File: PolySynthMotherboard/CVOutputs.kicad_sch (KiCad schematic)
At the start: 154 parts, among them U301 DAC7578xPW, U302 TL074, U303 TL072, U304 TMUX4051, U305 TL074, U306 TMUX4051, U307 TL074, U308 TMUX4051, U309 TMUX4051, U310 TL074, U311 TL074, U312 TL074, U313 TMUX4051, U314 TL074, U315 TL074, U316 TL074, U317 TMUX4051, U318 TMUX4051, U319 TL074, U320 TL072

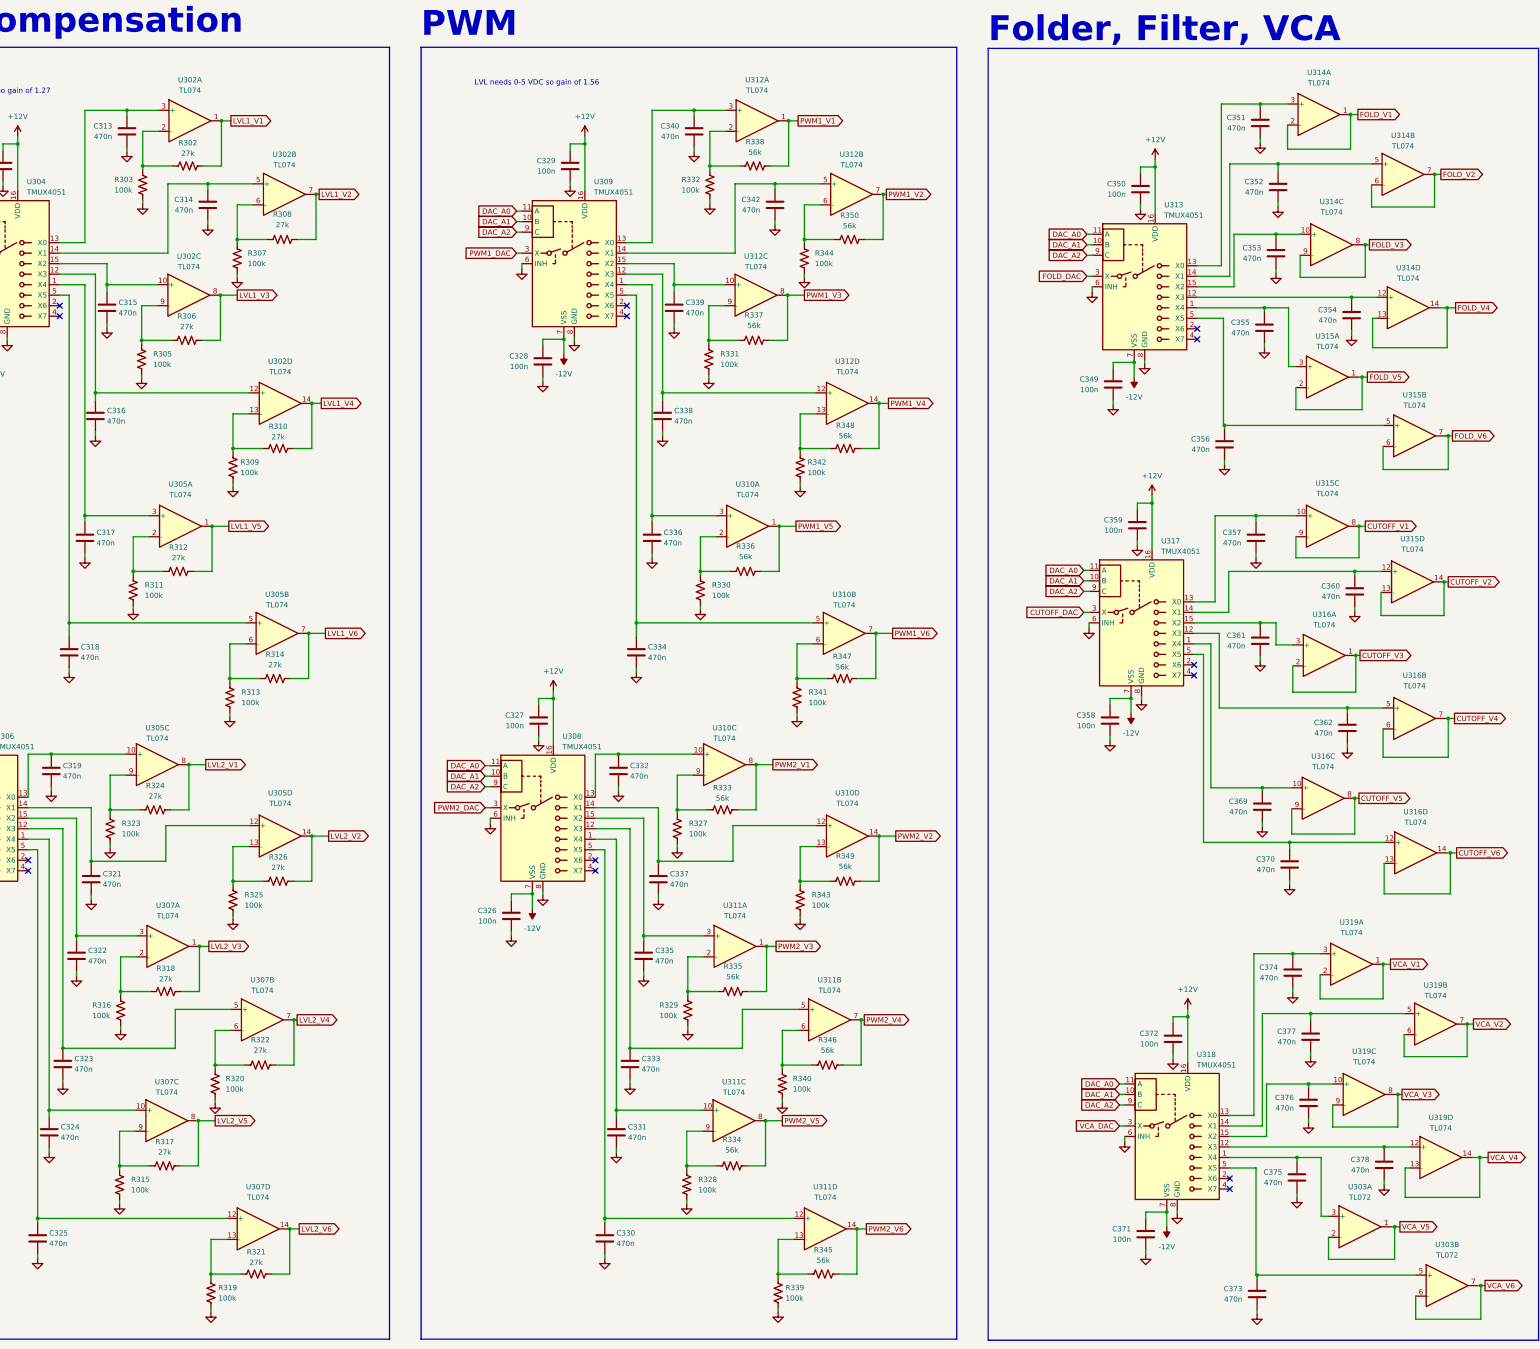
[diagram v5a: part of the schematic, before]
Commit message: op-amp layout improved
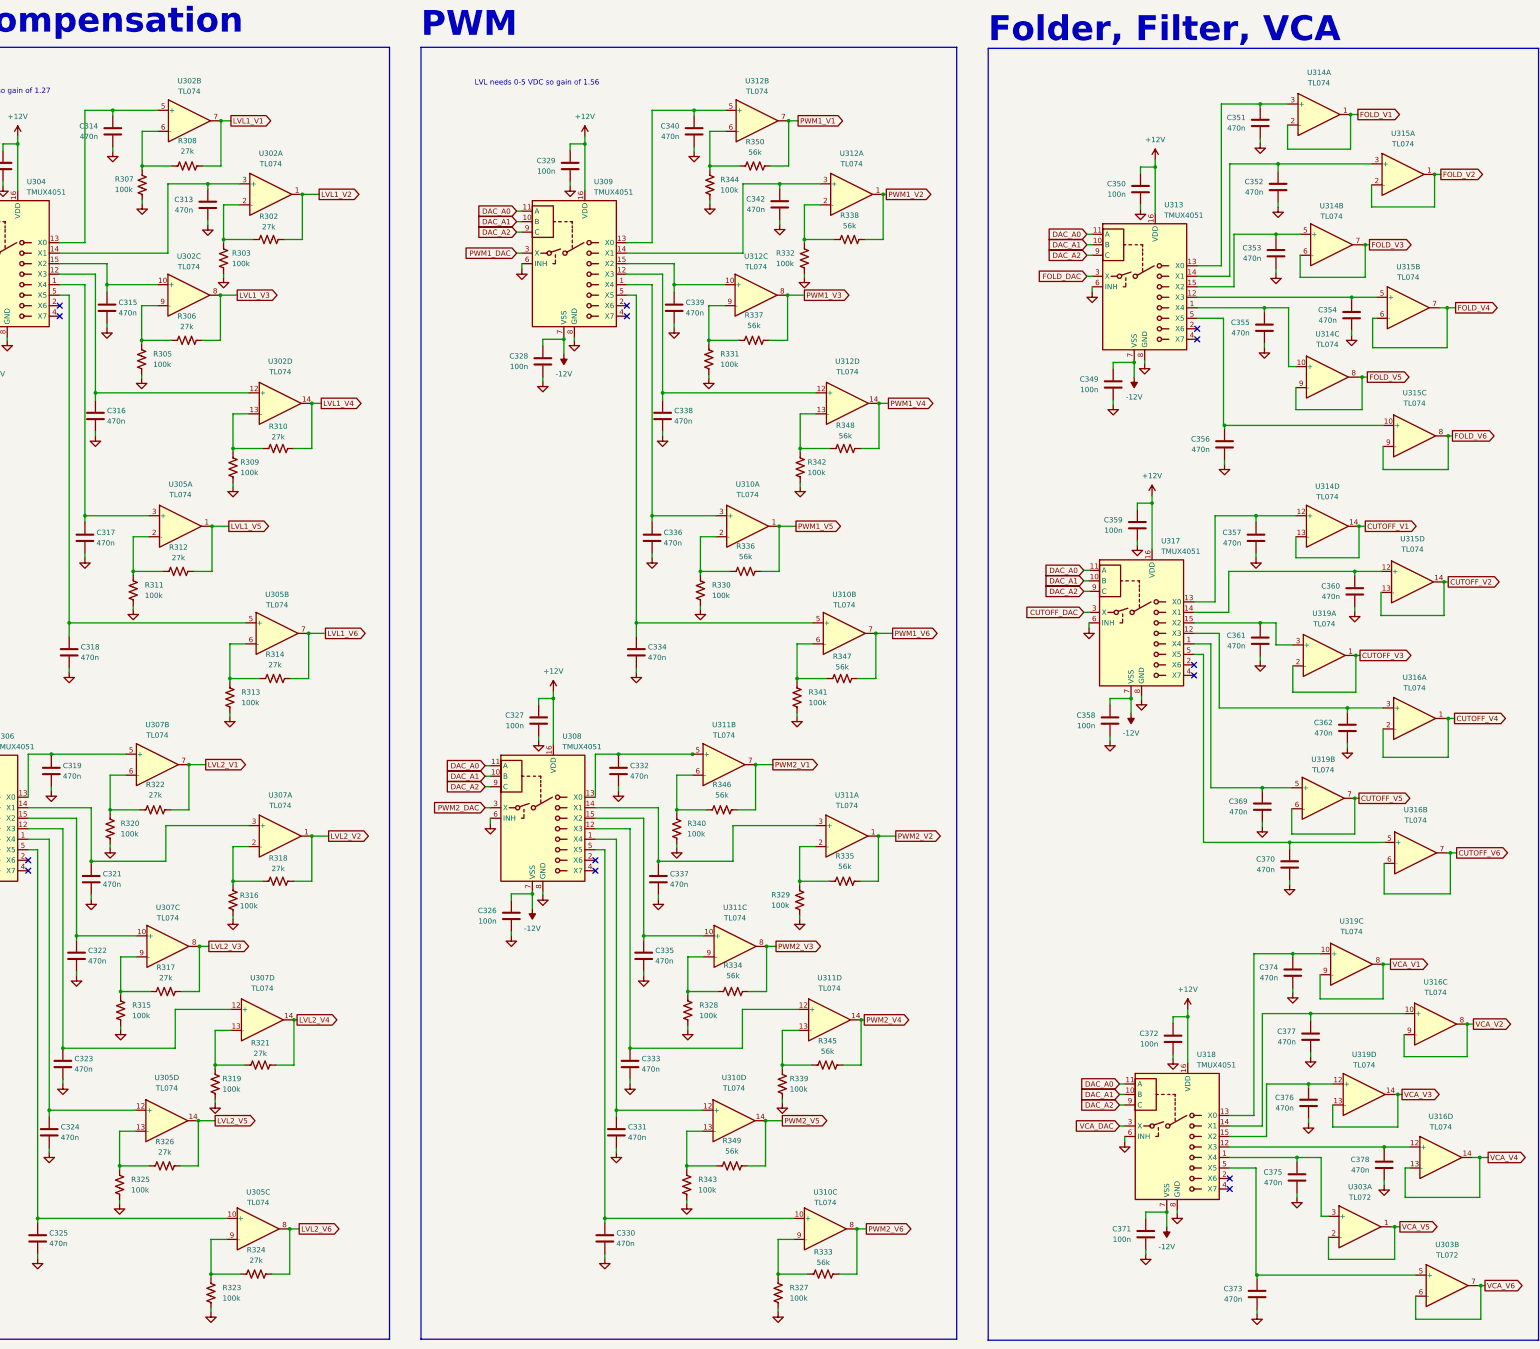
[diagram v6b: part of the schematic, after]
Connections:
- net CUTOFF_V1: now also U314.13 (-), U314.14; no longer U315.8, U315.9 (-)
- net CUTOFF_V3: now also U319.1, U319.2 (-); no longer U316.1, U316.2 (-)
- net CUTOFF_V4: now also U316.1, U316.2 (-); no longer U316.6 (-), U316.7
- net CUTOFF_V5: now also U319.6 (-), U319.7; no longer U316.8, U316.9 (-)
- net CUTOFF_V6: now also U316.6 (-), U316.7; no longer U316.13 (-), U316.14
- net FOLD_V2: now also U315.1, U315.2 (-); no longer U314.6 (-), U314.7
- net FOLD_V3: now also U314.6 (-), U314.7; no longer U314.8, U314.9 (-)
- net FOLD_V4: now also U315.6 (-), U315.7; no longer U314.13 (-), U314.14
- net FOLD_V5: now also U314.8, U314.9 (-); no longer U315.1, U315.2 (-)
- net FOLD_V6: now also U315.8, U315.9 (-); no longer U315.6 (-), U315.7
- net LVL1_V1: now also R308.2, U302.7; no longer R302.2, U302.1
- net LVL1_V2: now also R302.2, U302.1; no longer R308.2, U302.7
- net LVL2_V1: now also R322.2, U307.7; no longer R324.2, U305.8
- net LVL2_V2: now also R318.2, U307.1; no longer R326.2, U305.14
- net LVL2_V3: now also R317.2, U307.8; no longer R318.2, U307.1
- net LVL2_V4: now also R321.2, U307.14; no longer R322.2, U307.7
- net LVL2_V5: now also R326.2, U305.14; no longer R317.2, U307.8
- net LVL2_V6: now also R324.2, U305.8; no longer R321.2, U307.14
- net PWM1_V1: now also R350.2, U312.7; no longer R338.2, U312.1
- net PWM1_V2: now also R338.2, U312.1; no longer R350.2, U312.7
- net PWM2_V1: now also R346.2, U311.7; no longer R333.2, U310.8
- net PWM2_V2: now also R335.2, U311.1; no longer R349.2, U310.14
- net PWM2_V3: now also R334.2, U311.8; no longer R335.2, U311.1
- net PWM2_V4: now also R345.2, U311.14; no longer R346.2, U311.7
- net PWM2_V5: now also R349.2, U310.14; no longer R334.2, U311.8
- net PWM2_V6: now also R333.2, U310.8; no longer R345.2, U311.14
- net VCA_V1: now also U319.8, U319.9 (-); no longer U319.1, U319.2 (-)
- net VCA_V2: now also U316.8, U316.9 (-); no longer U319.6 (-), U319.7
- net VCA_V3: now also U319.13 (-), U319.14; no longer U319.8, U319.9 (-)
- net VCA_V4: now also U316.13 (-), U316.14; no longer U319.13 (-), U319.14
- net at C361.1, U317.15 (X2): now also U319.3 (+); no longer U316.3 (+)
- net at C321.1, U306.14 (X1): now also U307.3 (+); no longer U305.12 (+)
- net at C377.1, U318.14 (X1): now also U316.10 (+); no longer U319.5 (+)
- net at C314.1, U302.5 (+): now also U304.13 (X0); no longer U304.14 (X1)
- net at C322.1, U306.15 (X2): now also U307.10 (+); no longer U307.3 (+)
- net at C369.1, U317.1 (X4): now also U319.5 (+); no longer U316.10 (+)
- net at C352.1, U313.14 (X1): now also U315.3 (+); no longer U314.5 (+)
- net at C362.1, U317.12 (X3): now also U316.3 (+); no longer U316.5 (+)
- net at C330.1, U308.5 (X5): now also U310.10 (+); no longer U311.12 (+)
- net at C354.1, U313.12 (X3): now also U315.5 (+); no longer U314.12 (+)
- net at C356.1, U313.5 (X5): now also U315.10 (+); no longer U315.5 (+)
- net at C313.1, U302.3 (+): now also U304.14 (X1); no longer U304.13 (X0)
- net at C319.1, U306.13 (X0): now also U307.5 (+); no longer U305.10 (+)
- net at C324.1, U306.1 (X4): now also U305.12 (+); no longer U307.10 (+)
- net at C331.1, U308.1 (X4): now also U310.12 (+); no longer U311.10 (+)
- net at C335.1, U308.15 (X2): now also U311.10 (+); no longer U311.3 (+)
- net at C325.1, U306.5 (X5): now also U305.10 (+); no longer U307.12 (+)
- net at C337.1, U308.14 (X1): now also U311.3 (+); no longer U310.12 (+)
- net at C340.1, U309.13 (X0): now also U312.5 (+); no longer U312.3 (+)
- net at C323.1, U306.12 (X3): now also U307.12 (+); no longer U307.5 (+)
- net at C378.1, U318.12 (X3): now also U316.12 (+); no longer U319.12 (+)
- net at C374.1, U318.13 (X0): now also U319.10 (+); no longer U319.3 (+)
- net at C376.1, U318.15 (X2): now also U319.12 (+); no longer U319.10 (+)
- net at C353.1, U313.15 (X2): now also U314.5 (+); no longer U314.10 (+)
- net at C355.1, U313.1 (X4): now also U314.10 (+); no longer U315.3 (+)
- net at C342.1, U309.14 (X1): now also U312.3 (+); no longer U312.5 (+)
- net at C333.1, U308.12 (X3): now also U311.12 (+); no longer U311.5 (+)
- net at C370.1, U317.5 (X5): now also U316.5 (+); no longer U316.12 (+)
- net at C357.1, U317.13 (X0): now also U314.12 (+); no longer U315.10 (+)
- net at C332.1, U308.13 (X0): now also U311.5 (+); no longer U310.10 (+)
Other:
- moved on the sheet: C313, C314, C342, R302, R303, R307, R308, R315, R316, R317, R318, R319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

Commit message: power supply tweaks
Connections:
- net FOLD_V3: now also U314.8, U314.9 (-); no longer U314.6 (-), U314.7
- net FOLD_V5: now also U314.6 (-), U314.7; no longer U314.8, U314.9 (-)
- net GND: no longer U304.6 (INH), U306.6 (INH), U308.6 (INH), U309.6 (INH), U313.6 (INH), U317.6 (INH), U318.6 (INH)
- net PWM2_V1: now also R335.2, U311.1; no longer R346.2, U311.7
- net PWM2_V2: now also R346.2, U311.7; no longer R335.2, U311.1
- net PWM2_V3: now also R345.2, U311.14; no longer R334.2, U311.8
- net PWM2_V4: now also R334.2, U311.8; no longer R345.2, U311.14
- net at C353.1, U314.5 (+): now also U313.1 (X4); no longer U313.15 (X2)
- net at C333.1, U308.12 (X3): now also U311.10 (+); no longer U311.12 (+)
- net at C335.1, U308.15 (X2): now also U311.12 (+); no longer U311.10 (+)
- net at C337.1, U308.14 (X1): now also U311.5 (+); no longer U311.3 (+)
- net at C355.1, U314.10 (+): now also U313.15 (X2); no longer U313.1 (X4)
- net at C332.1, U308.13 (X0): now also U311.3 (+); no longer U311.5 (+)
- new net DAC_INH: U304.6 (INH), U306.6 (INH), U308.6 (INH), U309.6 (INH), U313.6 (INH), U317.6 (INH), U318.6 (INH)
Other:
- moved on the sheet: C353, C355, R328, R329, R334, R335, R339, R340, R345, R346, U311A, U311B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

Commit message: cleaned up CV opamps
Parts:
- removed R302, R306, R308, R310, R312, R314, R317, R318, R321, R322, R324, R326: 27k, PCM_Resistor_SMD_AKL:R_0805_2012Metric, symbol Device:R_US
- removed R303, R305, R307, R309, R311, R313, R315, R316, R319, R320, R323, R325, R327, R328, R329, R330, R331, R332, R339, R340, R341, R342, R343, R344: 100k, PCM_Resistor_SMD_AKL:R_0805_2012Metric, symbol Device:R_US
- removed R333, R334, R335, R336, R337, R338, R345, R346, R347, R348, R349, R350: 56k, PCM_Resistor_SMD_AKL:R_0805_2012Metric, symbol Device:R_US
- added C320, C341: 100n, Capacitor_SMD:C_0805_2012Metric, symbol Device:C
- added R351, R353, R355, R357: 100k, PCM_Resistor_SMD_AKL:R_0805_2012Metric, symbol Device:R_US
- added R352, R354: 27k, PCM_Resistor_SMD_AKL:R_0805_2012Metric, symbol Device:R_US
- added R356, R358: 56k, PCM_Resistor_SMD_AKL:R_0805_2012Metric, symbol Device:R_US
- added U321: TL074, Package_SO:SOIC-14_3.9x8.7mm_P1.27mm, symbol Amplifier_Operational:TL074
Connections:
- net +3.3VA is gone; now on net +3.3V: C301.1, C304.1, R304.1, U301.3 (AVDD)
- net +12V: now also C320.1, U321.4 (V+)
- net -12V: now also C341.1, U321.11 (V-)
- net CUTOFF_V1: now also U305.6 (-), U305.7; no longer U314.13 (-), U314.14
- net CUTOFF_V2: now also U310.6 (-), U310.7; no longer U315.13 (-), U315.14
- net CUTOFF_V3: now also U311.13 (-), U311.14; no longer U319.1, U319.2 (-)
- net CUTOFF_V4: now also U314.8, U314.9 (-); no longer U316.1, U316.2 (-)
- net CUTOFF_V5: now also U316.6 (-), U316.7; no longer U319.6 (-), U319.7
- net CUTOFF_V6: now also U319.13 (-), U319.14; no longer U316.6 (-), U316.7
- net FOLD_V1: now also U305.1, U305.2 (-); no longer U314.1, U314.2 (-)
- net FOLD_V2: now also U310.1, U310.2 (-); no longer U315.1, U315.2 (-)
- net FOLD_V3: now also U311.8, U311.9 (-); no longer U314.8, U314.9 (-)
- net FOLD_V4: now also U314.6 (-), U314.7; no longer U315.6 (-), U315.7
- net FOLD_V5: now also U316.1, U316.2 (-); no longer U314.6 (-), U314.7
- net FOLD_V6: now also U319.8, U319.9 (-); no longer U315.8, U315.9 (-)
- net GND: now also C320.2, C341.2, R351.1, R353.1, R355.1, R357.1
- net LVL1_DAC: now also R352.2, U321.1; no longer U301.4 (VOUTA)
- net LVL1_V1: now also U302.6 (-)
- net LVL1_V2: now also U307.1, U307.2 (-); no longer U302.1
- net LVL1_V3: now also U310.8, U310.9 (-); no longer U302.8
- net LVL1_V4: now also U312.6 (-), U312.7; no longer U302.14
- net LVL1_V5: now also U315.1, U315.2 (-); no longer U305.1
- net LVL1_V6: now also U316.8, U316.9 (-); no longer U305.7
- net LVL2_DAC: now also R354.2, U321.7; no longer U301.13 (VOUTB)
- net LVL2_V1: now also U302.1, U302.2 (-); no longer U307.7
- net LVL2_V2: now also U307.6 (-), U307.7; no longer U307.1
- net LVL2_V3: now also U310.13 (-), U310.14; no longer U307.8
- net LVL2_V4: now also U312.8, U312.9 (-); no longer U307.14
- net LVL2_V5: now also U315.6 (-), U315.7; no longer U305.14
- net LVL2_V6: now also U316.13 (-), U316.14; no longer U305.8
- net PWM1_DAC: now also R358.2, U321.14; no longer U301.5 (VOUTC)
- net PWM1_V1: now also U302.8, U302.9 (-); no longer U312.7
- net PWM1_V2: now also U307.8, U307.9 (-); no longer U312.1
- net PWM1_V3: now also U311.1, U311.2 (-); no longer U312.8
- net PWM1_V4: now also U312.13 (-)
- net PWM1_V5: now also U315.8, U315.9 (-); no longer U310.1
- net PWM1_V6: now also U319.1, U319.2 (-); no longer U310.7
- net PWM2_DAC: now also R356.2, U321.8; no longer U301.12 (VOUTD)
- net PWM2_V1: now also U302.13 (-), U302.14; no longer U311.1
- net PWM2_V2: now also U307.13 (-), U307.14; no longer U311.7
- net PWM2_V3: now also U311.6 (-), U311.7; no longer U311.14
- net PWM2_V4: now also U314.1, U314.2 (-); no longer U311.8
- net PWM2_V5: now also U315.13 (-), U315.14; no longer U310.14
- net PWM2_V6: now also U319.6 (-), U319.7; no longer U310.8
- net VCA_V1: now also U305.8, U305.9 (-); no longer U319.8, U319.9 (-)
- net VCA_V2: now also U305.13 (-), U305.14; no longer U316.8, U316.9 (-)
- net VCA_V3: now also U312.1, U312.2 (-); no longer U319.13 (-), U319.14
- net VCA_V4: now also U314.13 (-), U314.14; no longer U316.13 (-), U316.14
- net at C362.1, U317.12 (X3): now also U314.10 (+); no longer U316.3 (+)
- net at C324.1, U306.1 (X4): now also U315.5 (+); no longer U305.12 (+)
- net at C334.1, U309.5 (X5): now also U319.3 (+); no longer U310.5 (+)
- net at C369.1, U317.1 (X4): now also U316.5 (+); no longer U319.5 (+)
- net at C322.1, U306.15 (X2): now also U310.12 (+); no longer U307.10 (+)
- net at C353.1, U313.1 (X4): now also U316.3 (+); no longer U314.5 (+)
- net at C370.1, U317.5 (X5): now also U319.12 (+); no longer U316.5 (+)
- net at C335.1, U308.15 (X2): now also U311.5 (+); no longer U311.12 (+)
- net at C357.1, U317.13 (X0): now also U305.5 (+); no longer U314.12 (+)
- net at C360.1, U317.14 (X1): now also U310.5 (+); no longer U315.12 (+)
- net at C354.1, U313.12 (X3): now also U314.5 (+); no longer U315.5 (+)
- net at C313.1, U304.14 (X1): now also U307.3 (+); no longer U302.3 (+)
- net at C316.1, U304.12 (X3): now also U312.5 (+); no longer U302.12 (+)
- net at C325.1, U306.5 (X5): now also U316.12 (+); no longer U305.10 (+)
- net at C333.1, U308.12 (X3): now also U314.3 (+); no longer U311.10 (+)
- net at C336.1, U309.1 (X4): now also U315.10 (+); no longer U310.3 (+)
- net at C377.1, U318.14 (X1): now also U305.12 (+); no longer U316.10 (+)
- net at C323.1, U306.12 (X3): now also U312.10 (+); no longer U307.12 (+)
- net at C331.1, U308.1 (X4): now also U315.12 (+); no longer U310.12 (+)
- net at C339.1, U309.15 (X2): now also U311.3 (+); no longer U312.10 (+)
- net at C340.1, U309.13 (X0): now also U302.10 (+); no longer U312.5 (+)
- net at C337.1, U308.14 (X1): now also U307.12 (+); no longer U311.5 (+)
- net at C317.1, U304.1 (X4): now also U315.3 (+); no longer U305.3 (+)
- net at C378.1, U318.12 (X3): now also U314.12 (+); no longer U316.12 (+)
- net at C374.1, U318.13 (X0): now also U305.10 (+); no longer U319.10 (+)
- net at C376.1, U318.15 (X2): now also U312.3 (+); no longer U319.12 (+)
- net at C315.1, U304.15 (X2): now also U310.10 (+); no longer U302.10 (+)
- net at C330.1, U308.5 (X5): now also U319.5 (+); no longer U310.10 (+)
- net at C355.1, U313.15 (X2): now also U311.10 (+); no longer U314.10 (+)
- net at C352.1, U313.14 (X1): now also U310.3 (+); no longer U315.3 (+)
- net at C351.1, U313.13 (X0): now also U305.3 (+); no longer U314.3 (+)
- net at C342.1, U309.14 (X1): now also U307.10 (+); no longer U312.3 (+)
- net at C319.1, U306.13 (X0): now also U302.3 (+); no longer U307.5 (+)
- net at C321.1, U306.14 (X1): now also U307.5 (+); no longer U307.3 (+)
- net at C356.1, U313.5 (X5): now also U319.10 (+); no longer U315.10 (+)
- net at C361.1, U317.15 (X2): now also U311.12 (+); no longer U319.3 (+)
- net at C318.1, U304.5 (X5): now also U316.10 (+); no longer U305.5 (+)
- net at C332.1, U308.13 (X0): now also U302.12 (+); no longer U311.3 (+)
- new net: U301.12 (VOUTD), U321.10 (+)
- new net: R355.2, R356.1, U321.9 (-)
- new net: R353.2, R354.1, U321.6 (-)
- new net: U301.5 (VOUTC), U321.12 (+)
- new net: R357.2, R358.1, U321.13 (-)
- new net: R351.2, R352.1, U321.2 (-)
- new net: U301.13 (VOUTB), U321.5 (+)
- new net: U301.4 (VOUTA), U321.3 (+)
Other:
- note added: "LVL range: 0-4.191VDC (gain of 1.27) PWM range: 0-5VDC (gain of 1.5ish)"
- note removed: "LVL needs 0-4.2 VDC so gain of 1.27"
- note removed: "LVL needs 0-5 VDC so gain of 1.56"
- moved on the sheet: C302, C303, C305, C306, C307, C308, C309, C310, C311, C312, C313, C314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
